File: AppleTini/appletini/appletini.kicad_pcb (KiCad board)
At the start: 2 copper layers, 114.3 x 69.8 mm, 26 parts, among them J1 Conn_02x25_Counter_Clockwise, Q1 DMG2305UX-7, U1 74LS245, U16 Pico, U17 Teensy4.1, U2 74LS245, U3 74LS245, U4 74LS245, U5 74LVC1G07, U6 74LVC1G07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

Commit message: fix some ground issues
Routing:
- net GND: track 0.00 -> 59.3 mm, vias 2 -> 4

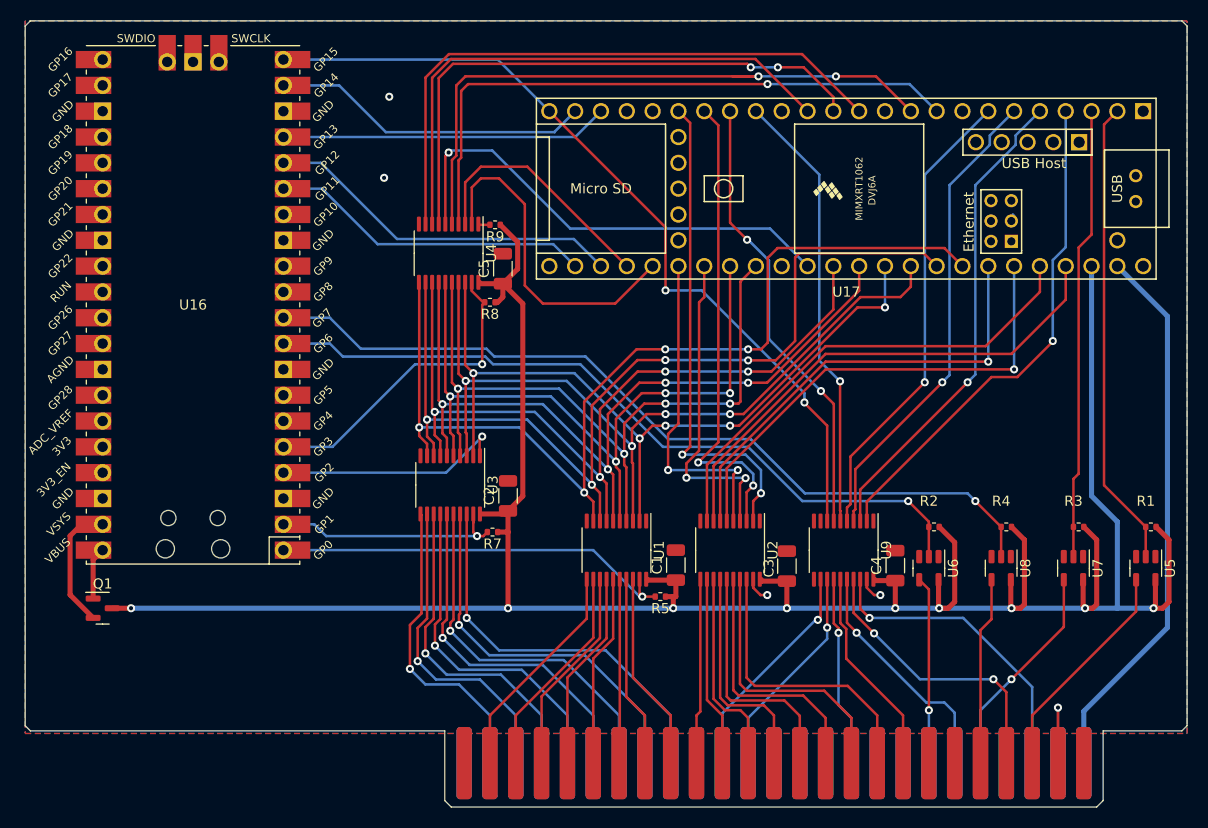
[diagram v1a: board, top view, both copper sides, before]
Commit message: Changed to use single LVC07 Shrink vias to 0.6mm Spaced vias further apart Increased zone fill
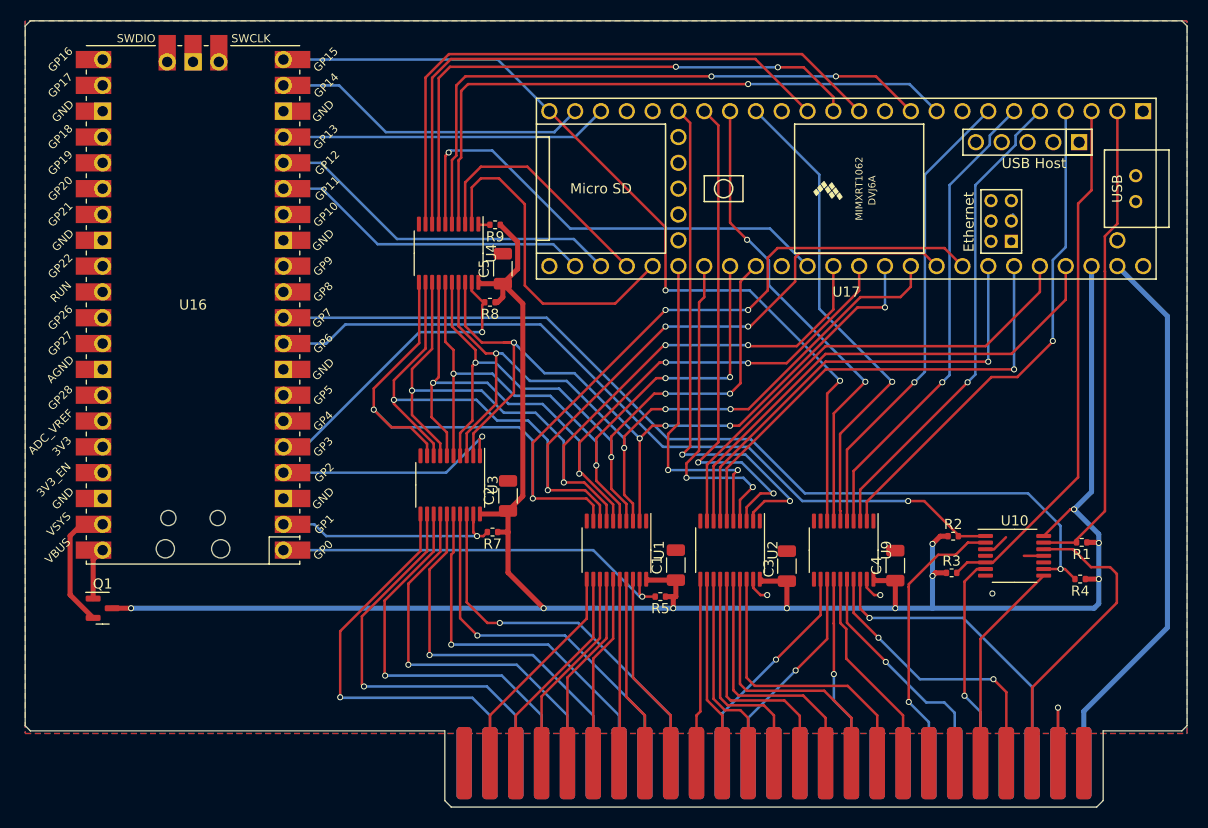
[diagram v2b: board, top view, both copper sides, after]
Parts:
- removed U5, U6, U7, U8: 74LVC1G07, Package_TO_SOT_SMD:SOT-23-5
- added U10: 74LS07, Package_SO:TSSOP-14_4.4x5mm_P0.65mm, F.Cu at (173.5, 116.1)
- moved R3 13.3 mm to (167.3, 117.8), turned to 0 degrees
- moved R4 8.89 mm to (180.0, 118.4)
- moved R1 6.97 mm to (180.1, 114.8)
- moved R2 2.09 mm to (167.5, 114.2), turned to 0 degrees
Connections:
- J1 pad 25: +5V -> unconnected-(J1-Pin_25-Pad25)
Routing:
- net +3.3V: track 252.7 -> 215.5 mm, vias 9 -> 10
- net /Transceivers/ALO_D0: track 97.5 -> 110.9 mm
- net /BUS_D0: track 30.2 -> 41.5 mm
- net /RDY: track 82.1 -> 92.7 mm
- net /BUS_INH: track 18.4 -> 27.7 mm
- net /BUS_D1: track 31.4 -> 40.5 mm
- net /BUS_INTOUT: track 22.3 -> 30.3 mm
- net /Transceivers/ALO_D2: track 78.9 -> 86.9 mm
- net /Transceivers/ALO_D1: track 93.5 -> 101.5 mm
- net /IRQ: track 44.6 -> 52.4 mm
- net /BUS_D2: track 32.7 -> 39.6 mm
- net /BUS_D3: track 33.7 -> 38.5 mm
- net GND: track 59.3 -> 63.8 mm, vias 4 -> 3
- net /INH: track 74.4 -> 78.7 mm
- net /M2B0: track 43.8 -> 48.0 mm
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
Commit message: move vias farther from pads
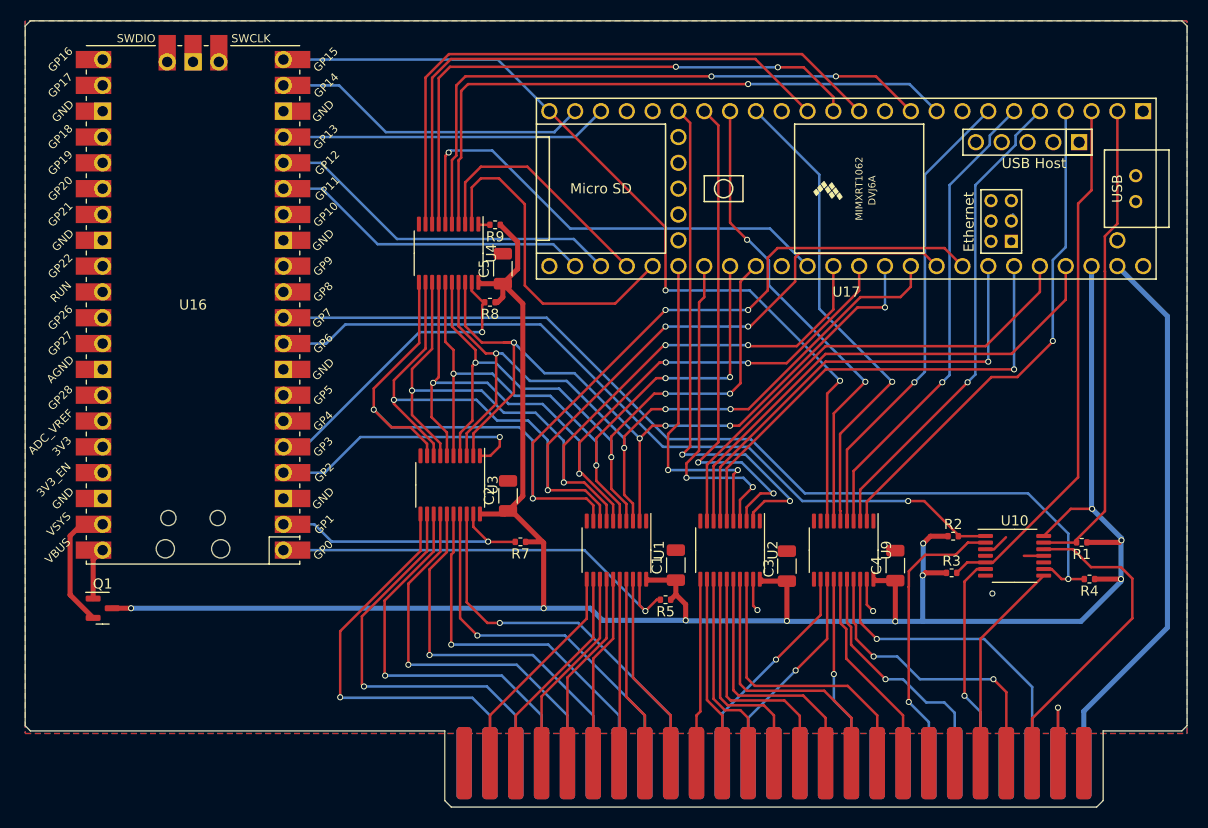
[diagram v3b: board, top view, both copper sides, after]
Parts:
- moved R7 2.91 mm to (124.9, 114.8)
- moved R4 0.92 mm to (180.9, 118.4)
- moved R5 0.59 mm to (139.2, 120.4)
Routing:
- net +3.3V: track 215.5 -> 230.4 mm
- net /D_EN: track 23.1 -> 26.8 mm
- net /ALO_EN: track 40.3 -> 43.4 mm
- net /D_DIR: track 23.0 -> 26.0 mm
- net /RDY: track 92.7 -> 94.9 mm
- net /BUS_INTOUT: track 30.3 -> 32.2 mm
- net GND: track 63.8 -> 65.4 mm
- net /BUS_DMA: track 28.6 -> 29.9 mm
- net /BUS_RES: track 23.5 -> 24.5 mm
- net /BUS_INTIN: track 30.5 -> 31.3 mm
- net /BUS_INH: track 27.7 -> 28.4 mm

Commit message: Caps on bus power lines
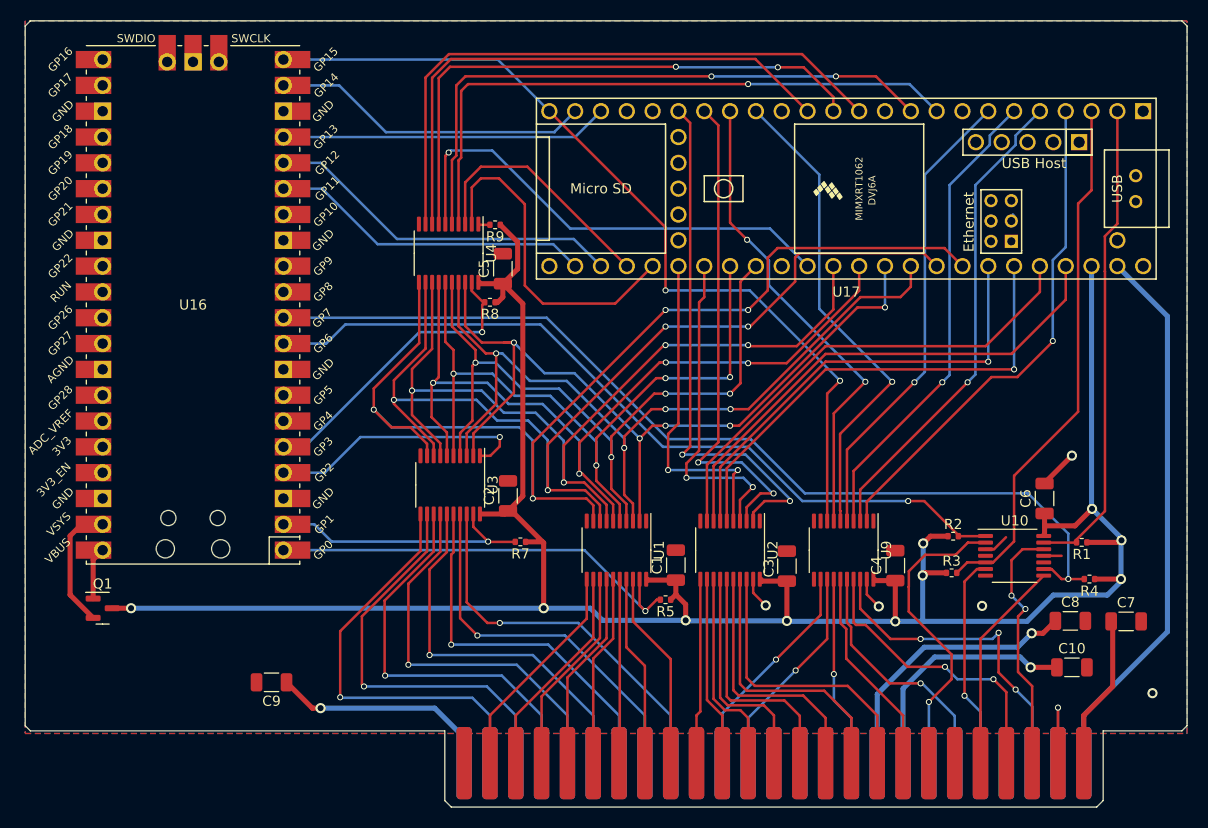
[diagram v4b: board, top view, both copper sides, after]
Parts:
- added C10: 0.1uF, Capacitor_SMD:C_1206_3216Metric, F.Cu at (179.2, 127.1)
- added C6: 0.1uF, Capacitor_SMD:C_1206_3216Metric, F.Cu at (176.5, 110.5)
- added C7: 0.1uF, Capacitor_SMD:C_1206_3216Metric, F.Cu at (184.5, 122.6)
- added C8: 0.1uF, Capacitor_SMD:C_1206_3216Metric, F.Cu at (179.0, 122.5)
- added C9: 0.1uF, Capacitor_SMD:C_1206_3216Metric, F.Cu at (100.4, 128.6)
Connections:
- J1 pad 25: unconnected-(J1-Pin_25-Pad25) -> +5V
- J1 pad 33: unconnected-(J1-Pin_33-Pad33) -> -12V
- J1 pad 34: unconnected-(J1-Pin_34-Pad34) -> -5V
- J1 pad 50: unconnected-(J1-Pin_50-Pad50) -> +12V
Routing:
- net -5V: track 0.00 -> 27.3 mm, vias 0 -> 1
- net -12V: track 0.00 -> 24.2 mm, vias 0 -> 1
- net +12V: track 0.00 -> 22.3 mm, vias 0 -> 1
- net +5V: track 0.00 -> 15.2 mm
- net /BUS_INTOUT: track 32.2 -> 25.1 mm, vias 0 -> 2
- net GND: track 65.4 -> 68.7 mm, vias 3 -> 5
- net /BUS_INH: track 28.4 -> 30.3 mm
- net +3.3V: track 230.4 -> 232.1 mm
- net /BUS_INTIN: track 31.3 -> 32.2 mm, vias 1 -> 3
- net /BUS_DMA: track 29.9 -> 29.1 mm
